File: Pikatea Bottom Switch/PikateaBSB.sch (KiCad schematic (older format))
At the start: 5 parts

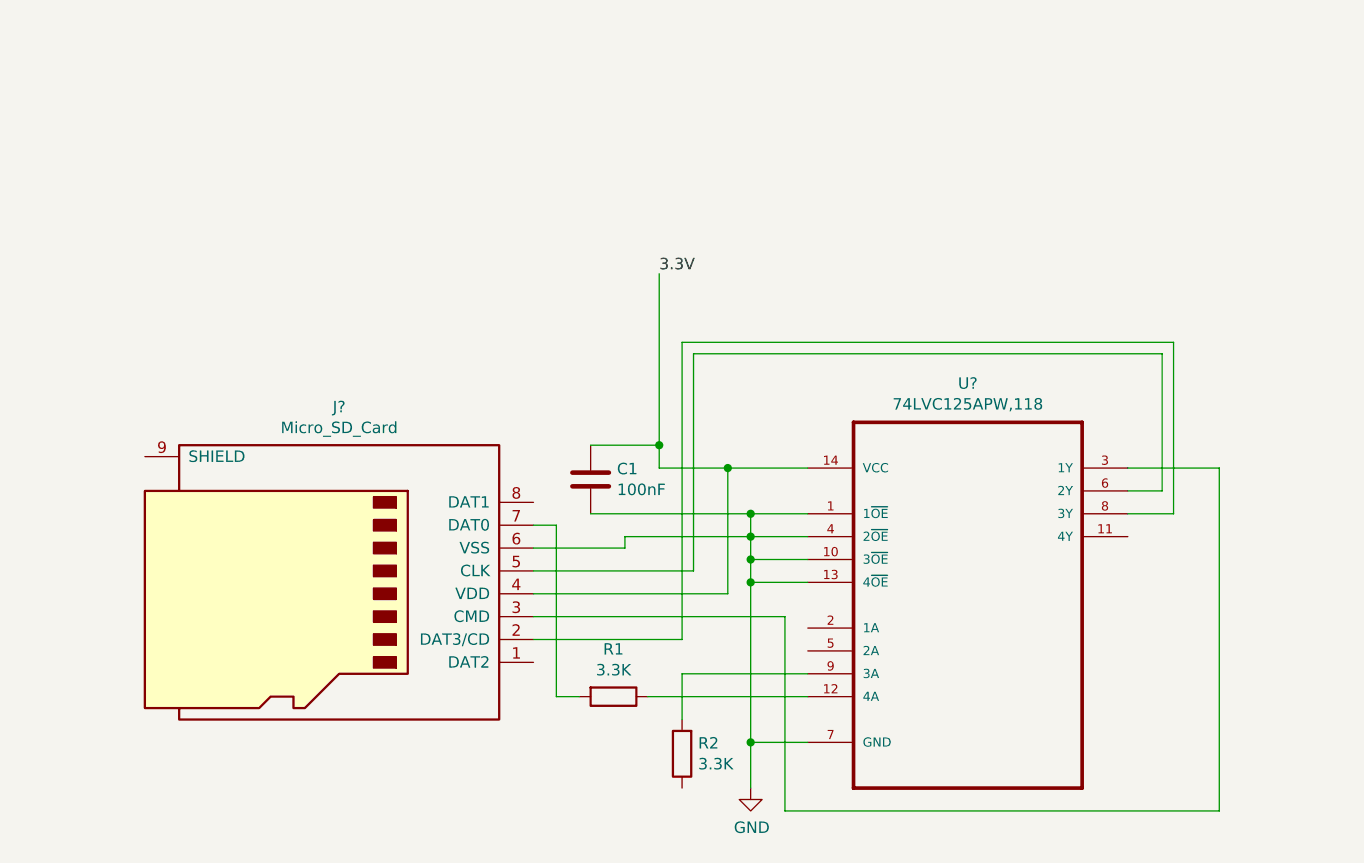
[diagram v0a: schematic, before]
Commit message: Beginings of SD card part of the board
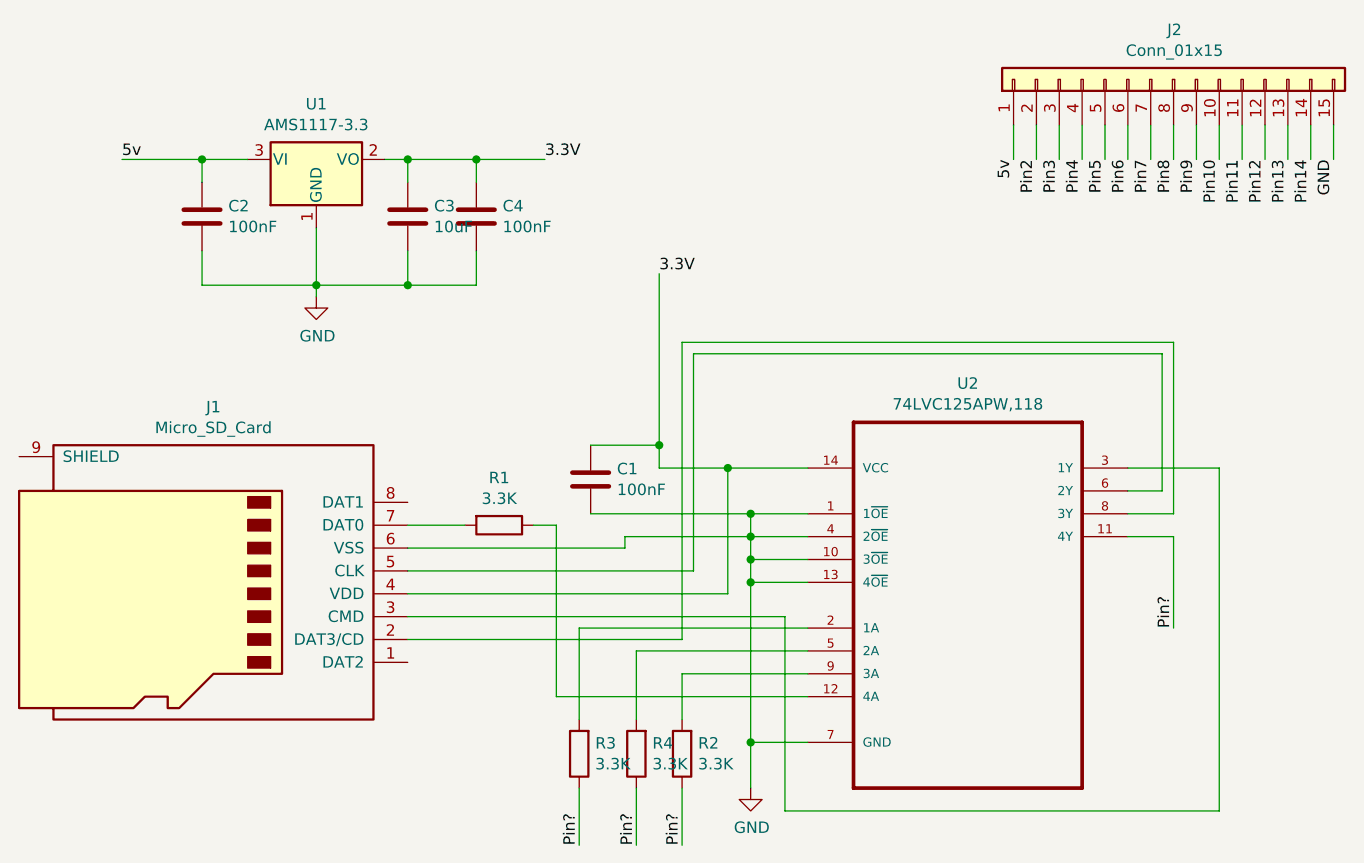
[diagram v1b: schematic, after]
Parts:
- added C2, C4: 100nF, Capacitor_SMD:C_0805_2012Metric, symbol Device:C
- added C3: 10uF, Capacitor_SMD:C_0805_2012Metric, symbol Device:C
- added J2: Conn_01x15, Connector_PinHeader_2.54mm:PinHeader_1x15_P2.54mm_Vertical, symbol Connector_Generic:Conn_01x15
- added R3, R4: 3.3K, Resistor_SMD:R_0805_2012Metric, symbol Device:R
- added U1: AMS1117-3.3, Package_TO_SOT_SMD:SOT-223-3_TabPin2, symbol Regulator_Linear:AMS1117-3.3
- C1: footprint (none) -> Capacitor_SMD:C_0805_2012Metric
- J1: renamed from J?; footprint (none) -> Connector_Card:microSD_HC_Molex_104031-0811
- R1, R2: footprint (none) -> Resistor_SMD:R_0805_2012Metric
- U2: renamed from U?; footprint SOP65P640X110-14N -> Package_SO:TSSOP-14-1EP_4.4x5mm_P0.65mm
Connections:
- net 3.3V: now also C3.1, C4.1, U1.2 (VO)
- net GND: now also C2.2, C3.2, C4.2, J2.15 (Pin_15), U1.1 (GND)
- net Pin?: now reaches U2.11 (4Y)
- net Pin?: now also R2.1, R3.1, R4.1
- net at U2.2 (1A): now also R3.2
- net at U2.5 (2A): now also R4.2
- new net 5v: C2.1, J2.1 (Pin_1), U1.3 (VI)
- new net Pin10: J2.10 (Pin_10)
- new net Pin11: J2.11 (Pin_11)
- new net Pin12: J2.12 (Pin_12)
- new net Pin13: J2.13 (Pin_13)
- new net Pin14: J2.14 (Pin_14)
- new net Pin2: J2.2 (Pin_2)
- new net Pin3: J2.3 (Pin_3)
- new net Pin4: J2.4 (Pin_4)
- new net Pin5: J2.5 (Pin_5)
- new net Pin6: J2.6 (Pin_6)
- new net Pin7: J2.7 (Pin_7)
- new net Pin8: J2.8 (Pin_8)
- new net Pin9: J2.9 (Pin_9)
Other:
- moved on the sheet: J1, R1

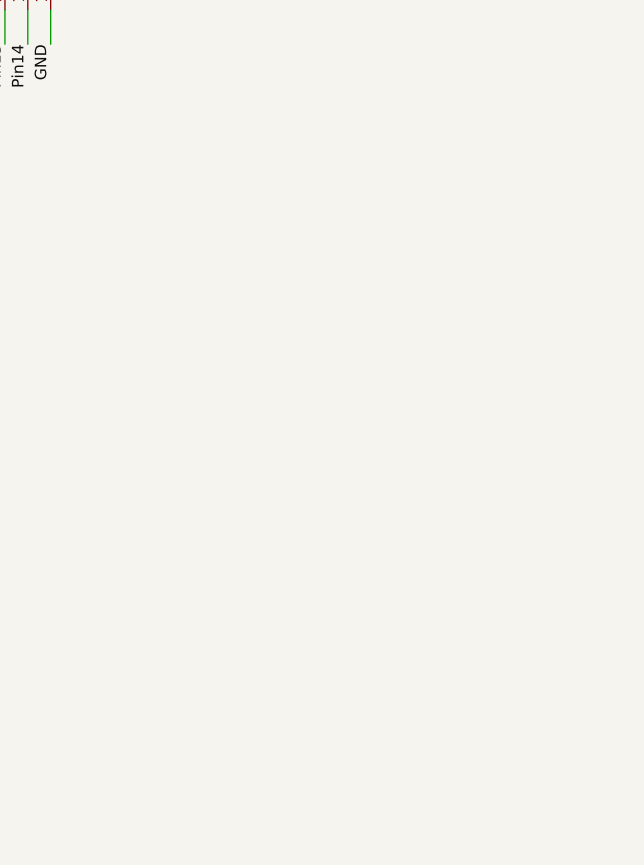
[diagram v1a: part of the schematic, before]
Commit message: added some useful keyboard libraries. added footprints to board
schematic still needs to be finished
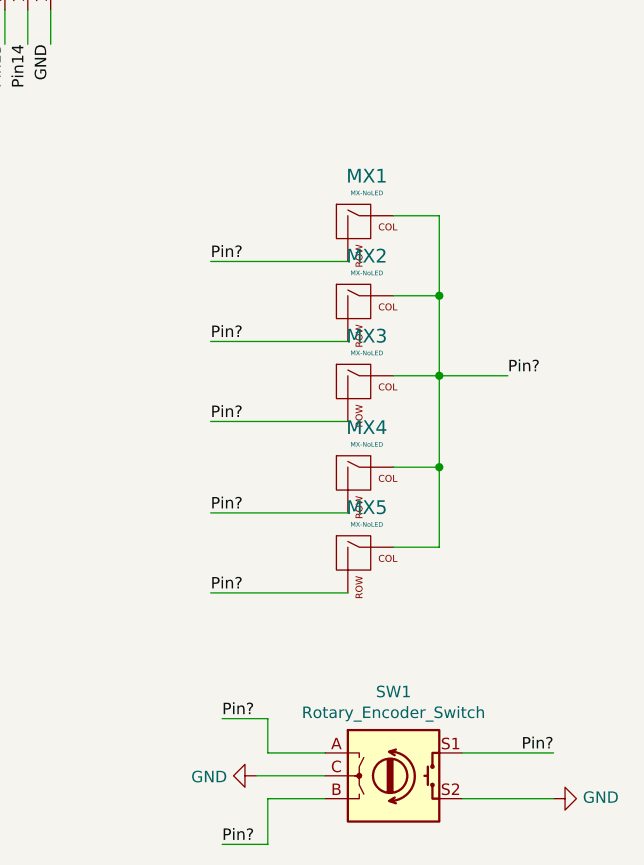
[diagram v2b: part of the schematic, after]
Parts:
- added MX1, MX2, MX3, MX4, MX5: MX-NoLED, MX_Alps_Hybrid:MX-1U, symbol MX_Alps_Hybrid:MX-NoLED
- added SW1: Rotary_Encoder_Switch, Rotary_Encoder:RotaryEncoder_Alps_EC12E-Switch_Vertical_H20mm, symbol Device:Rotary_Encoder_Switch
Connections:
- net GND: now also SW1.C, SW1.S2
- net Pin?: now also MX1.1 (COL), MX1.2 (ROW), MX2.1 (COL), MX2.2 (ROW), MX3.1 (COL), MX3.2 (ROW), MX4.1 (COL), MX4.2 (ROW), MX5.1 (COL), MX5.2 (ROW), SW1.A, SW1.B, SW1.S1
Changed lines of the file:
@@
 Wire Wire Line
 	2900 1700 2500 1700
+Text Label 7650 3550 0    50   ~ 0
+Pin?
+Text Label 7650 3200 0    50   ~ 0
+Pin?
+Text Label 7650 2800 0    50   ~ 0
+Pin?
+Text Label 7650 2450 0    50   ~ 0
+Pin?
+Text Label 7650 2100 0    50   ~ 0
+Pin?
+Wire Wire Line
+	8250 2100 7650 2100
+Wire Wire Line
+	8250 2450 7650 2450
+Wire Wire Line
+	8250 2800 7650 2800
+Wire Wire Line
+	8250 3550 7650 3550
+Text Label 8950 2600 0    50   ~ 0
+Pin?
+$Comp
+L Device:Rotary_Encoder_Switch SW1
+U 1 1 5F07F9BA
+P 8450 4350
+F 0 "SW1" H 8450 4717 50  0000 C CNN
+F 1 "Rotary_Encoder_Switch" H 8450 4626 50  0000 C CNN
+F 2 "Rotary_Encoder:RotaryEncoder_Alps_EC12E-Switch_Vertical_H20mm" H 8300 4510 50  0001 C CNN
+F 3 "~" H 8450 4610 50  0001 C CNN
+	1    8450 4350
+	1    0    0    -1
+$EndComp
+Wire Wire Line
+	9150 4250 8750 4250
+$Comp
+L power:GND #PWR0103
+U 1 1 5F083C63
+P 7850 4350
+F 0 "#PWR0103" H 7850 4100 50  0001 C CNN
+F 1 "GND" V 7855 4222 50  0000 R CNN
+F 2 "" H 7850 4350 50  0001 C CNN
+F 3 "" H 7850 4350 50  0001 C CNN
+	1    7850 4350
+	0    1    1    0
+$EndComp
+Wire Wire Line
+	7850 4350 8150 4350
+Text Label 7700 4100 0    50   ~ 0
+Pin?
+Text Label 7700 4650 0    50   ~ 0
+Pin?
+Wire Wire Line
+	8150 4250 7900 4250
+Wire Wire Line
+	7900 4250 7900 4100
+Wire Wire Line
+	7900 4100 7700 4100
+Wire Wire Line
+	8150 4450 7900 4450
+Wire Wire Line
+	7900 4450 7900 4650
+Wire Wire Line
+	7900 4650 7700 4650
+Text Label 9150 4250 2    50   ~ 0
+Pin?
+$Comp
+L power:GND #PWR0104
+U 1 1 5F08DC47
+P 9150 4450
+F 0 "#PWR0104" H 9150 4200 50  0001 C CNN
+F 1 "GND" V 9155 4322 50  0000 R CNN
+F 2 "" H 9150 4450 50  0001 C CNN
+F 3 "" H 9150 4450 50  0001 C CNN
+	1    9150 4450
+	0    -1   -1   0
+$EndComp
+Wire Wire Line
+	9150 4450 8750 4450
+$Comp
+L MX_Alps_Hybrid:MX-NoLED MX1
+U 1 1 5F096095
+P 8300 1950
+F 0 "MX1" H 8333 2173 60  0000 C CNN
+F 1 "MX-NoLED" H 8333 2099 20  0000 C CNN
+F 2 "MX_Alps_Hybrid:MX-1U" H 7675 1925 60  0001 C CNN
+F 3 "" H 7675 1925 60  0001 C CNN
+	1    8300 1950
+	1    0    0    -1
+$EndComp
+$Comp
+L MX_Alps_Hybrid:MX-NoLED MX2
+U 1 1 5F096A04
+P 8300 2300
+F 0 "MX2" H 8333 2523 60  0000 C CNN
+F 1 "MX-NoLED" H 8333 2449 20  0000 C CNN
+F 2 "MX_Alps_Hybrid:MX-1U" H 7675 2275 60  0001 C CNN
+F 3 "" H 7675 2275 60  0001 C CNN
+	1    8300 2300
+	1    0    0    -1
+$EndComp
+$Comp
+L MX_Alps_Hybrid:MX-NoLED MX3
+U 1 1 5F096DF4
+P 8300 2650
+F 0 "MX3" H 8333 2873 60  0000 C CNN
+F 1 "MX-NoLED" H 8333 2799 20  0000 C CNN
+F 2 "MX_Alps_Hybrid:MX-1U" H 7675 2625 60  0001 C CNN
+F 3 "" H 7675 2625 60  0001 C CNN
+	1    8300 2650
+	1    0    0    -1
+$EndComp
+Wire Wire Line
+	7650 3200 8250 3200
+$Comp
+L MX_Alps_Hybrid:MX-NoLED MX4
+U 1 1 5F097C77
+P 8300 3050
+F 0 "MX4" H 8333 3273 60  0000 C CNN
+F 1 "MX-NoLED" H 8333 3199 20  0000 C CNN
+F 2 "MX_Alps_Hybrid:MX-1U" H 7675 3025 60  0001 C CNN
+F 3 "" H 7675 3025 60  0001 C CNN
+	1    8300 3050
+	1    0    0    -1
+$EndComp
+$Comp
+L MX_Alps_Hybrid:MX-NoLED MX5
+U 1 1 5F098026
+P 8300 3400
+F 0 "MX5" H 8333 3623 60  0000 C CNN
+F 1 "MX-NoLED" H 8333 3549 20  0000 C CNN
+F 2 "MX_Alps_Hybrid:MX-1U" H 7675 3375 60  0001 C CNN
+F 3 "" H 7675 3375 60  0001 C CNN
+	1    8300 3400
+	1    0    0    -1
+$EndComp
+Wire Wire Line
+	8450 3350 8650 3350
+Wire Wire Line
+	8650 3350 8650 3000
+Wire Wire Line
+	8650 3000 8450 3000
+Wire Wire Line
+	8650 3000 8650 2600
+Wire Wire Line
+	8650 2600 8450 2600
+Connection ~ 8650 3000
+Wire Wire Line
+	8650 2600 8650 2250
+Wire Wire Line
+	8650 2250 8450 2250
+Connection ~ 8650 2600
+Wire Wire Line
+	8650 2250 8650 1900
+Wire Wire Line
+	8650 1900 8450 1900
+Connection ~ 8650 2250
+Wire Wire Line
+	8950 2600 8650 2600
 $EndSCHEMATC

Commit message: Bottom Switch plate, footprints in place
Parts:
- removed J1: Micro_SD_Card, Connector_Card:microSD_HC_Molex_104031-0811, symbol Connector:Micro_SD_Card
- removed J2: Conn_01x15, Connector_PinHeader_2.54mm:PinHeader_1x15_P2.54mm_Vertical, symbol Connector_Generic:Conn_01x15
- added J1: Conn_01x16, Connector_PinHeader_2.54mm:PinHeader_1x16_P2.54mm_Vertical, symbol Connector_Generic:Conn_01x16
- added J2, J3: Conn_01x03, Connector_PinHeader_2.54mm:PinHeader_1x03_P2.54mm_Vertical, symbol Connector_Generic:Conn_01x03
- added XS1: SD_ebay-uSD-push_push_SMD, Sd-Card:Conn_uSDcard, symbol uSD_push-push_ebay:SD_ebay-uSD-push_push_SMD
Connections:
- net labels added: A0, CS, D2, D3, D4, D5, D6, D7, D8, D9, MISO, MOSI, RESET, SCK
- net labels removed: Pin10, Pin11, Pin12, Pin13, Pin14, Pin2, Pin3, Pin4, Pin5, Pin6, Pin7, Pin8, Pin9, Pin?
- wire segments 106 -> 136
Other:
- moved on the sheet: MX1, MX2, MX3, MX4, MX5

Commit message: Update Doughter board
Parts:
- added SW2: SW_DPST, Button_Switch_THT:SW_PUSH_6mm, symbol Switch:SW_DPST
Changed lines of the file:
@@
 Text Label 9900 1150 0    50   ~ 0
 D5
+$Comp
+L Switch:SW_DPST SW2
+U 1 1 5F12BE9E
+P 7700 2150
+F 0 "SW2" H 7700 2475 50  0000 C CNN
+F 1 "SW_DPST" H 7700 2384 50  0000 C CNN
+F 2 "Button_Switch_THT:SW_PUSH_6mm" H 7700 2150 50  0001 C CNN
+F 3 "~" H 7700 2150 50  0001 C CNN
+	1    7700 2150
+	1    0    0    -1
+$EndComp
+Text Label 7900 2050 0    50   ~ 0
+RESET
+Text Label 7500 2050 2    50   ~ 0
+GND
 $EndSCHEMATC

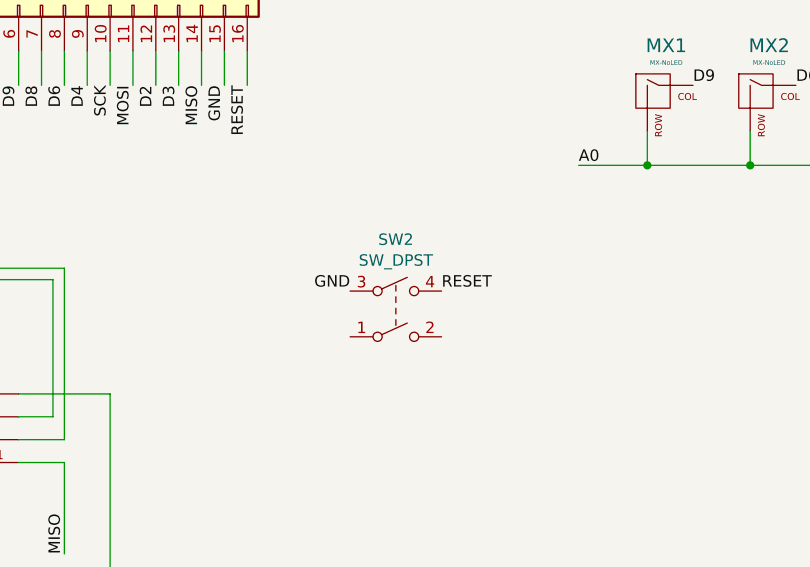
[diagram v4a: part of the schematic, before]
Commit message: added circuit board cutouts
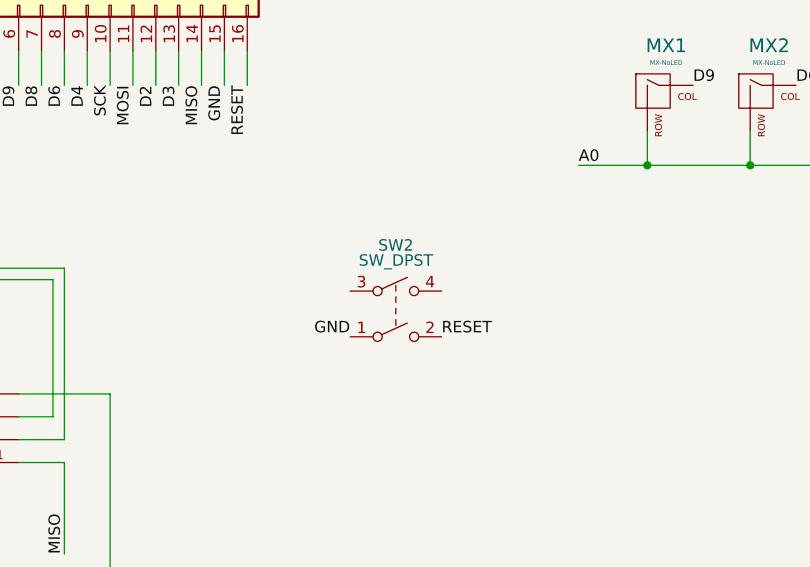
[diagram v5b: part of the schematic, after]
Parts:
- SW2: footprint Button_Switch_THT:SW_PUSH_6mm -> Button_Switch_SMD:SW_SPST_TL3342
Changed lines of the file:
@@
 U 1 1 5F12BE9E
 P 7700 2150
-F 0 "SW2" H 7700 2475 50  0000 C CNN
+F 0 "SW2" H 7700 2450 50  0000 C CNN
 F 1 "SW_DPST" H 7700 2384 50  0000 C CNN
-F 2 "Button_Switch_THT:SW_PUSH_6mm" H 7700 2150 50  0001 C CNN
+F 2 "Button_Switch_SMD:SW_SPST_TL3342" H 7700 2150 50  0001 C CNN
 F 3 "~" H 7700 2150 50  0001 C CNN
 	1    7700 2150
 	1    0    0    -1
 $EndComp
-Text Label 7900 2050 0    50   ~ 0
+Text Label 7900 2250 0    50   ~ 0
 RESET
-Text Label 7500 2050 2    50   ~ 0
+Text Label 7500 2250 2    50   ~ 0
 GND
 $EndSCHEMATC
